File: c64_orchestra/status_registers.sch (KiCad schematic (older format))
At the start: 3 parts

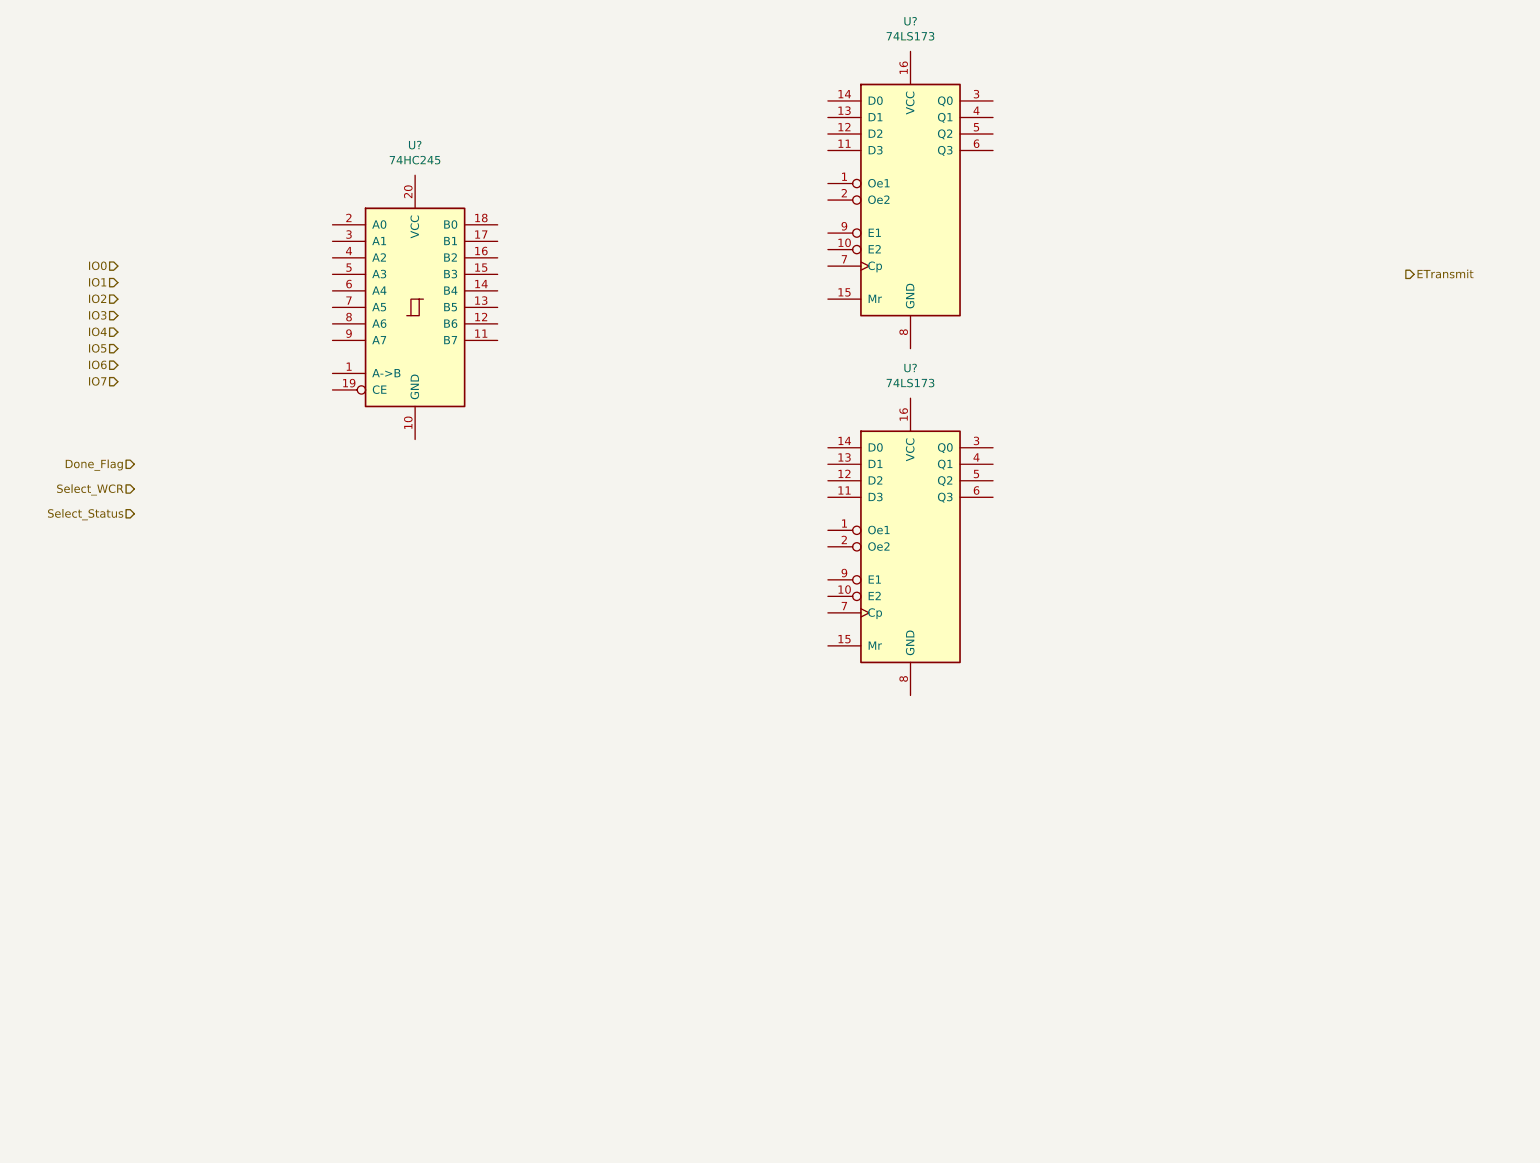
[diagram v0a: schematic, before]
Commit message: Added parts of schematic and worked on pcb layout.
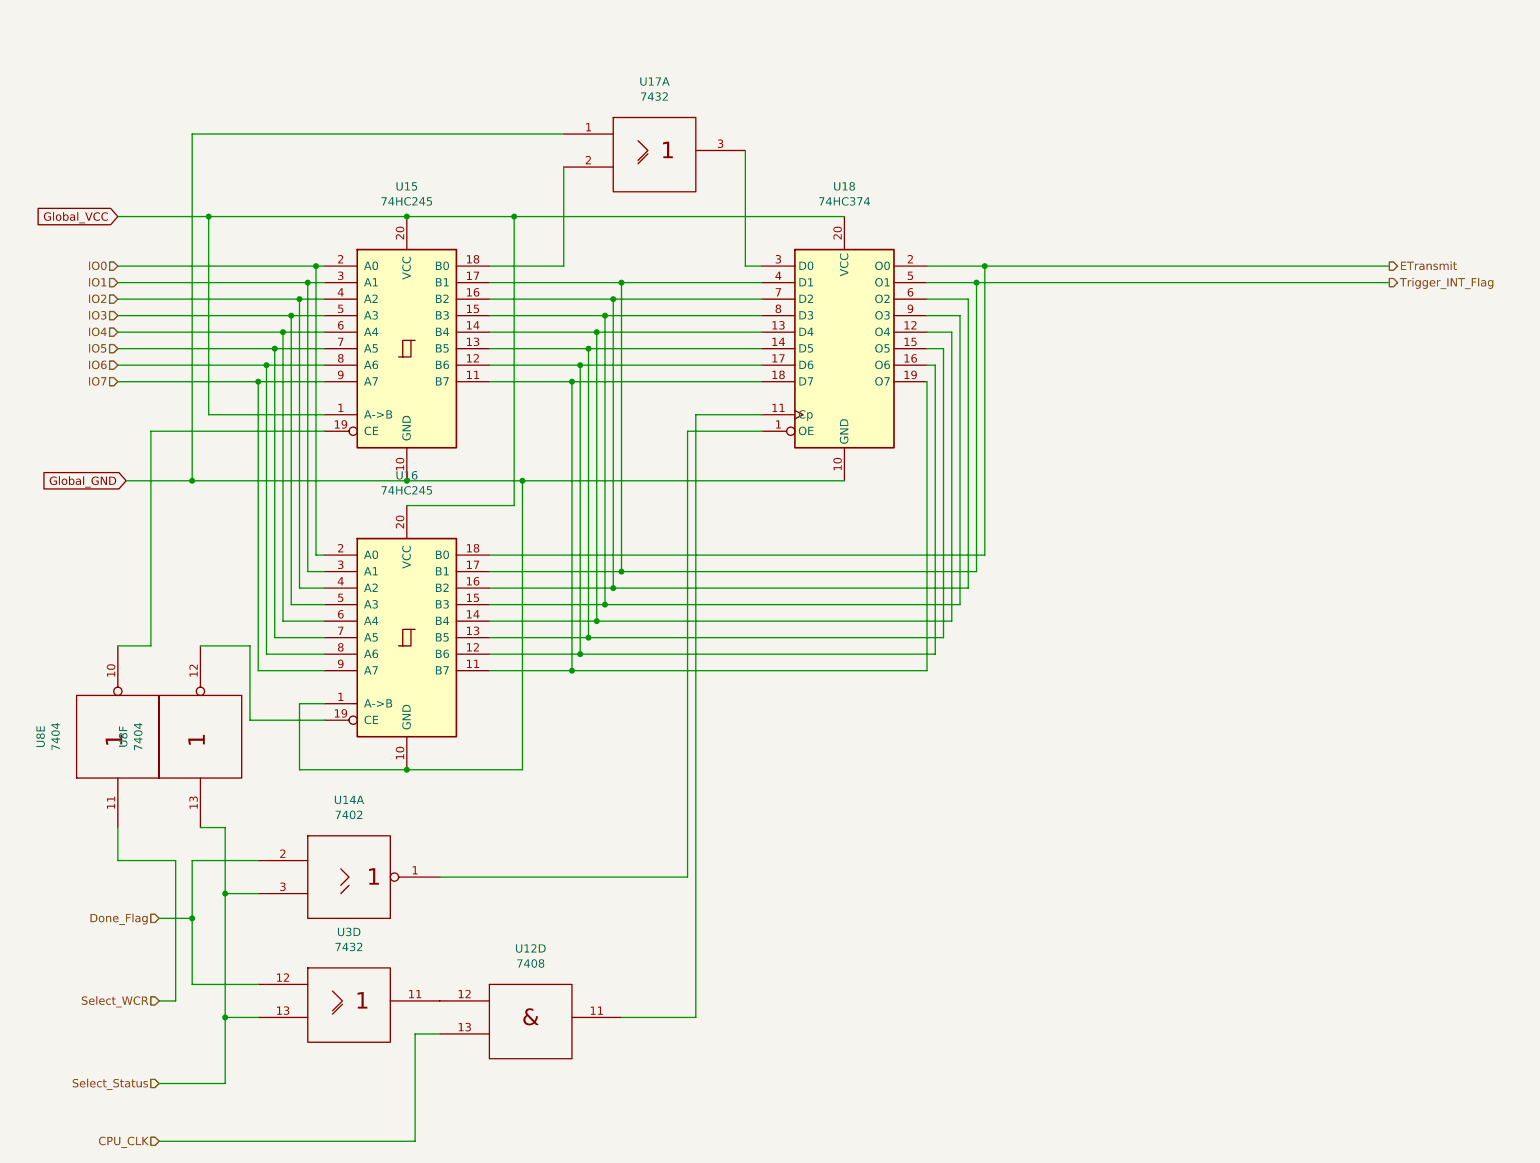
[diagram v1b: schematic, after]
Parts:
- removed U?: 74HC245, symbol 74xx:74HC245
- removed U? (x2): 74LS173, symbol 74xx:74LS173
- added U12: 7408, Package_DIP:DIP-14_W7.62mm, symbol 74xx_IEEE:7408
- added U14: 7402, Package_DIP:DIP-14_W7.62mm, symbol 74xx_IEEE:7402
- added U15, U16: 74HC245, Package_DIP:DIP-20_W7.62mm, symbol 74xx:74HC245
- added U17, U3: 7432, Package_DIP:DIP-14_W7.62mm, symbol 74xx_IEEE:7432
- added U18: 74HC374, Package_DIP:DIP-20_W7.62mm, symbol 74xx:74HC374
- added U8: 7404, Package_DIP:DIP-12_W10.16mm, symbol 74xx_IEEE:7404
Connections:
- net Done_Flag: now also U14.2, U3.12
- net ETransmit: now also U16.18 (B0), U18.2 (O0)
- net IO0: now also U15.2 (A0), U16.2 (A0)
- net IO1: now also U15.3 (A1), U16.3 (A1)
- net IO2: now also U15.4 (A2), U16.4 (A2)
- net IO3: now also U15.5 (A3), U16.5 (A3)
- net IO4: now also U15.6 (A4), U16.6 (A4)
- net IO5: now also U15.7 (A5), U16.7 (A5)
- net IO6: now also U15.8 (A6), U16.8 (A6)
- net IO7: now also U15.9 (A7), U16.9 (A7)
- net Select_Status: now also U14.3, U3.13, U8.13
- net Select_WCR: now also U8.11
- new net: U14.1, U18.1 (OE)
- new net: U12.11, U18.11 (Cp)
- new net: U15.14 (B4), U16.14 (B4), U18.12 (O4), U18.13 (D4)
- new net: U15.13 (B5), U16.13 (B5), U18.14 (D5), U18.15 (O5)
- new net: U15.12 (B6), U16.12 (B6), U18.16 (O6), U18.17 (D6)
- new net: U15.11 (B7), U16.11 (B7), U18.18 (D7), U18.19 (O7)
- new net: U17.3, U18.3 (D0)
- new net: U15.16 (B2), U16.16 (B2), U18.6 (O2), U18.7 (D2)
- new net: U15.15 (B3), U16.15 (B3), U18.8 (D3), U18.9 (O3)
- new net: U15.18 (B0), U17.2
- new net: U15.19 (CE), U8.10
- new net: U16.19 (CE), U8.12
- new net: U12.12, U3.11
- new net CPU_CLK: U12.13
- new net GND: U14.7 (GND)
- new net Global_GND: U15.10 (GND), U16.1 (A->B), U16.10 (GND), U17.1, U18.10 (GND)
- new net Global_VCC: U15.1 (A->B), U15.20 (VCC), U16.20 (VCC), U18.20 (VCC)
- new net Gnd: U12.14 (Vcc), U12.7 (Gnd), U17.14 (Vcc), U17.7 (Gnd), U3.14 (Vcc), U3.7 (Gnd), U8.14 (Vcc), U8.14 (Vcc), U8.7 (Gnd), U8.7 (Gnd)
- new net Trigger_INT_Flag: U15.17 (B1), U16.17 (B1), U18.4 (D1), U18.5 (O1)
- new net VCC: U14.14 (VCC)

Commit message: Changed the logic gates' numbering, changed some gates for todos.
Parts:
- removed U12: 7408, Package_DIP:DIP-14_W7.62mm, symbol 74xx_IEEE:7408
- removed U14: 7402, Package_DIP:DIP-14_W7.62mm, symbol 74xx_IEEE:7402
- removed U17, U3: 7432, Package_DIP:DIP-14_W7.62mm, symbol 74xx_IEEE:7432
- added U? (x2): 7432, symbol 74xx_IEEE:7432
- added U?: 7404, symbol 74xx_IEEE:7404
- added U?: 7408, symbol 74xx_IEEE:7408
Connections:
- net CPU_CLK: now also U?.10
- net Done_Flag: now also U?.9
- net Global_GND: now also U?.4
- net Gnd: now also U?.14 (Vcc), U?.14 (Vcc), U?.14 (Vcc), U?.14 (Vcc), U?.7 (Gnd), U?.7 (Gnd), U?.7 (Gnd), U?.7 (Gnd)
- net Select_Status: now also U?.10
- net at U18.1 (OE): now also U?.8
- net at U18.11 (Cp): now also U?.8
- net at U18.3 (D0): now also U?.6
- net at U15.18 (B0): now also U?.5
- new net: U?.8, U?.9, U?.9
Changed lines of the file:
@@
 Wire Wire Line
 	4000 3900 3200 3900
-$Comp
-L 74xx_IEEE:7432 U17
-U 1 1 5F9BFD33
-P 4200 1350
-F 0 "U17" H 4200 1766 50  0000 C CNN
-F 1 "7432" H 4200 1675 50  0000 C CNN
-F 2 "Package_DIP:DIP-14_W7.62mm" H 4200 1350 50  0001 C CNN
-F 3 "" H 4200 1350 50  0001 C CNN
-	1    4200 1350
-	1    0    0    -1
-$EndComp
 Wire Wire Line
 	950  1750 1500 1750
@@
 Wire Wire Line
 	1400 3350 1400 1250
-Wire Wire Line
-	1400 1250 3650 1250
 Connection ~ 1400 3350
 Wire Wire Line
@@
 	0    -1   -1   0
 $EndComp
-$Comp
-L 74xx_IEEE:7402 U14
-U 1 1 5FA7360B
-P 2350 5750
-F 0 "U14" H 2350 6216 50  0000 C CNN
-F 1 "7402" H 2350 6125 50  0000 C CNN
-F 2 "Package_DIP:DIP-14_W7.62mm" H 2350 5750 50  0001 C CNN
-F 3 "" H 2350 5750 50  0001 C CNN
-	1    2350 5750
-	1    0    0    -1
-$EndComp
 Wire Wire Line
 	1600 7000 1600 6600
 Wire Wire Line
-	1600 5850 1800 5850
-Wire Wire Line
 	1200 6000 1400 6000
 Wire Wire Line
-	1400 6000 1400 5650
-Wire Wire Line
-	1400 5650 1800 5650
-Wire Wire Line
 	4850 3050 4400 3050
 Wire Wire Line
-	4400 3050 4400 5750
-Wire Wire Line
-	4400 5750 2900 5750
-$Comp
-L 74xx_IEEE:7432 U3
-U 4 1 5FA89DE8
-P 2350 6500
-F 0 "U3" H 2350 6916 50  0000 C CNN
-F 1 "7432" H 2350 6825 50  0000 C CNN
-F 2 "Package_DIP:DIP-14_W7.62mm" H 2350 6500 50  0001 C CNN
-F 3 "" H 2350 6500 50  0001 C CNN
-	4    2350 6500
-	1    0    0    -1
-$EndComp
-Wire Wire Line
 	1400 6000 1400 6400
 Wire Wire Line
 	1400 6400 1800 6400
-Connection ~ 1400 6000
 Wire Wire Line
 	1600 6600 1800 6600
 Connection ~ 1600 6600
-Wire Wire Line
-	1600 6600 1600 5850
 Text HLabel 1200 7350 0    50   Input ~ 0
 CPU_CLK
-$Comp
-L 74xx_IEEE:7408 U12
-U 4 1 5FA9ABE7
-P 3450 6600
-F 0 "U12" H 3450 7016 50  0000 C CNN
-F 1 "7408" H 3450 6925 50  0000 C CNN
-F 2 "Package_DIP:DIP-14_W7.62mm" H 3450 6600 50  0001 C CNN
-F 3 "" H 3450 6600 50  0001 C CNN
-	4    3450 6600
-	1    0    0    -1
-$EndComp
 Wire Wire Line
 	1200 7350 2750 7350
@@
 	2750 7350 2750 6700
 Wire Wire Line
-	2750 6700 2900 6700
-Wire Wire Line
-	4000 6600 4450 6600
+	4350 6600 4450 6600
 Wire Wire Line
 	4450 6600 4450 2950
@@
 	1200 7000 1600 7000
 Wire Wire Line
-	1600 5850 1600 5450
-Wire Wire Line
 	1600 5450 1450 5450
-Connection ~ 1600 5850
 Wire Wire Line
 	1200 6500 1300 6500
@@
 	6150 2150 8650 2150
 Connection ~ 6150 2150
+$Comp
+L 74xx_IEEE:7404 U?
+U 4 1 5F959C37
+P 3800 5850
+F 0 "U?" H 3800 6316 50  0000 C CNN
+F 1 "7404" H 3800 6225 50  0000 C CNN
+F 2 "" H 3800 5850 50  0001 C CNN
+F 3 "" H 3800 5850 50  0001 C CNN
+	4    3800 5850
+	1    0    0    -1
+$EndComp
+Wire Wire Line
+	4400 5850 4350 5850
+Wire Wire Line
+	4400 3050 4400 5850
+Wire Wire Line
+	3250 5850 3050 5850
+Wire Wire Line
+	3050 5850 3050 6500
+Wire Wire Line
+	2900 6500 3050 6500
+Connection ~ 3050 6500
+Wire Wire Line
+	3050 6500 3250 6500
+Wire Wire Line
+	2750 6700 3250 6700
+Wire Wire Line
+	1600 5450 1600 6600
+Wire Wire Line
+	1400 1250 3650 1250
+$Comp
+L 74xx_IEEE:7432 U?
+U 2 1 5F916FED
+P 4200 1350
+F 0 "U?" H 4200 1766 50  0000 C CNN
+F 1 "7432" H 4200 1675 50  0000 C CNN
+F 2 "" H 4200 1350 50  0001 C CNN
+F 3 "" H 4200 1350 50  0001 C CNN
+	2    4200 1350
+	1    0    0    -1
+$EndComp
+$Comp
+L 74xx_IEEE:7432 U?
+U 3 1 5F94F15B
+P 2350 6500
+F 0 "U?" H 2350 6916 50  0000 C CNN
+F 1 "7432" H 2350 6825 50  0000 C CNN
+F 2 "" H 2350 6500 50  0001 C CNN
+F 3 "" H 2350 6500 50  0001 C CNN
+	3    2350 6500
+	1    0    0    -1
+$EndComp
+$Comp
+L 74xx_IEEE:7408 U?
+U 3 1 5F975E95
+P 3800 6600
+F 0 "U?" H 3800 7016 50  0000 C CNN
+F 1 "7408" H 3800 6925 50  0000 C CNN
+F 2 "" H 3800 6600 50  0001 C CNN
+F 3 "" H 3800 6600 50  0001 C CNN
+	3    3800 6600
+	1    0    0    -1
+$EndComp
 $EndSCHEMATC
